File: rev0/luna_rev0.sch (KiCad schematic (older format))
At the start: 35 parts, among them J1 USB_B_Micro, J2 USB_B_Micro, J3 USB_A, J4 USB_B_Micro, J7 Conn_02x02_Counter_Clockwise, J8 Conn_Coaxial, J9 Conn_Coaxial, SW1 BTN_RECOVERY, SW2 BTN_DFU, SW3 BTN_RESET, U1 AP22814-SOT, U12 AP22814-SOT, Y1 DSC60xx

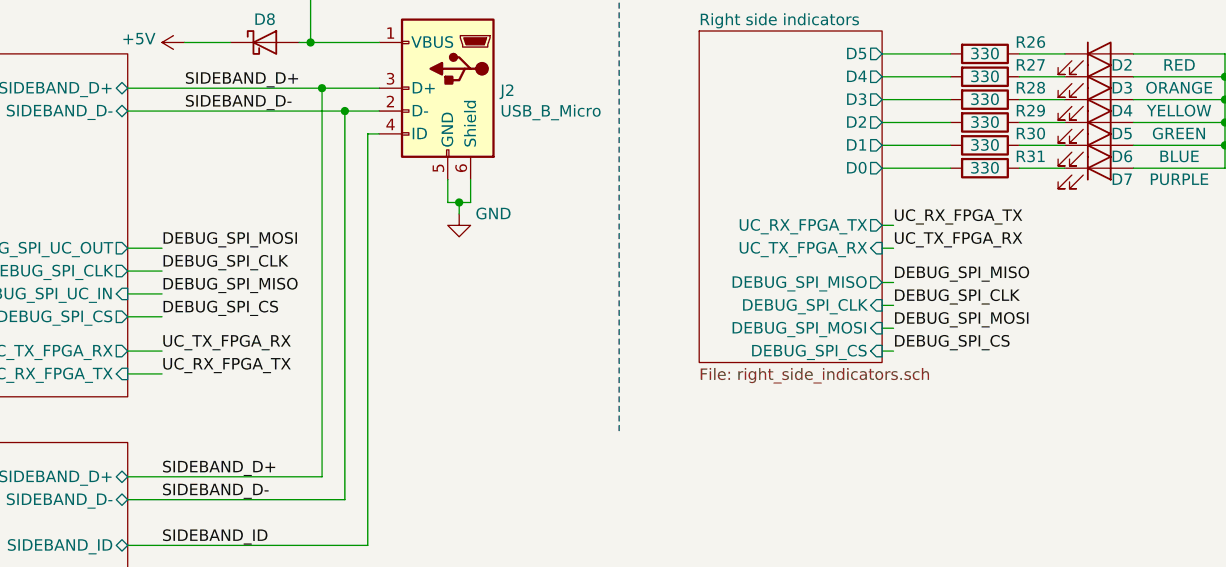
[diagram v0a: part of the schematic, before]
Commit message: hardware: adopt OSHWA convention for SPI signal names
https://www.oshwa.org/a-resolution-to-redefine-spi-signal-names
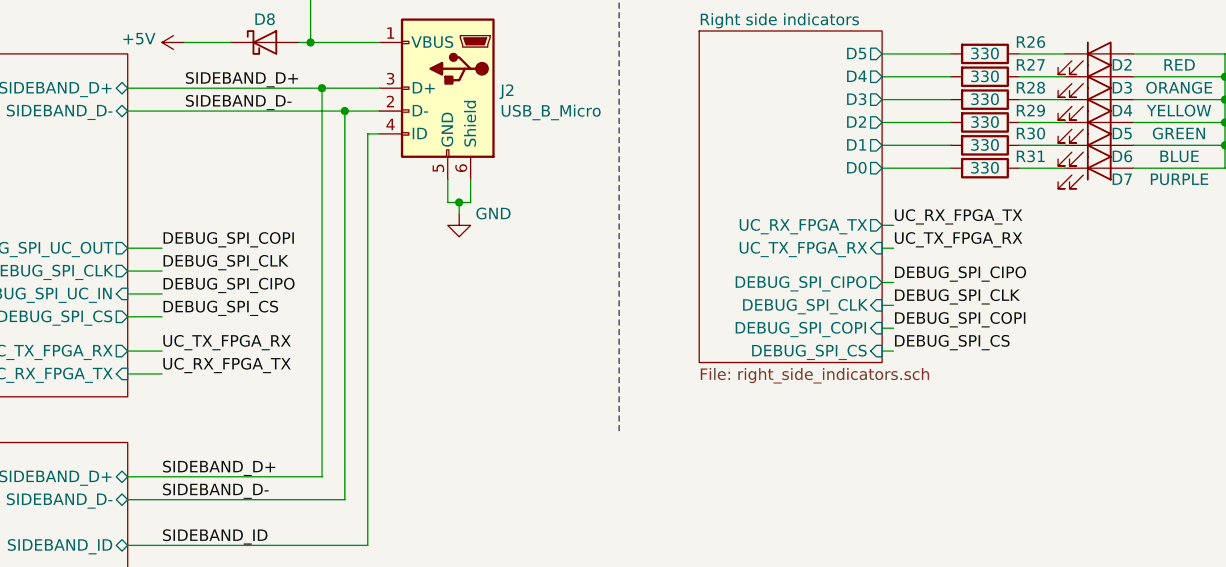
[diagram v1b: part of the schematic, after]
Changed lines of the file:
@@
 	5700 5750 5850 5750
 Text Label 5850 5750 0    50   ~ 0
-DEBUG_SPI_MOSI
+DEBUG_SPI_COPI
 Wire Wire Line
 	5700 5850 5850 5850
@@
 	5700 5950 5850 5950
 Text Label 5850 5950 0    50   ~ 0
-DEBUG_SPI_MISO
+DEBUG_SPI_CIPO
 Text Label 5850 5850 0    50   ~ 0
 DEBUG_SPI_CLK
@@
 TARGET_FAULT
 Text Label 9050 6100 0    50   ~ 0
-DEBUG_SPI_MOSI
+DEBUG_SPI_COPI
 $Comp
 L Device:R R26
@@
 F8 "UC_RX_FPGA_TX" O R 9000 5650 50
 F9 "UC_TX_FPGA_RX" I R 9000 5750 50
-F10 "DEBUG_SPI_MISO" O R 9000 5900 50
+F10 "DEBUG_SPI_CIPO" O R 9000 5900 50
 F11 "DEBUG_SPI_CLK" I R 9000 6000 50
-F12 "DEBUG_SPI_MOSI" I R 9000 6100 50
+F12 "DEBUG_SPI_COPI" I R 9000 6100 50
 F13 "DEBUG_SPI_CS" I R 9000 6200 50
 $EndSheet
@@
 DEBUG_SPI_CLK
 Text Label 9050 5900 0    50   ~ 0
-DEBUG_SPI_MISO
+DEBUG_SPI_CIPO
 Text Label 9050 6200 0    50   ~ 0
 DEBUG_SPI_CS

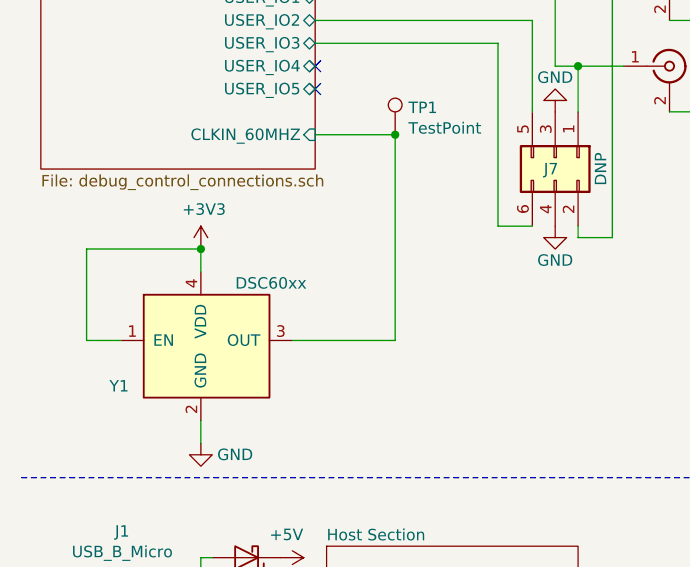
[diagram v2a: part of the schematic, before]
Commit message: hardware: replace Y1 DSC6001MI2A-060.0000 with SIT1602BC-73-33E-60.000000E
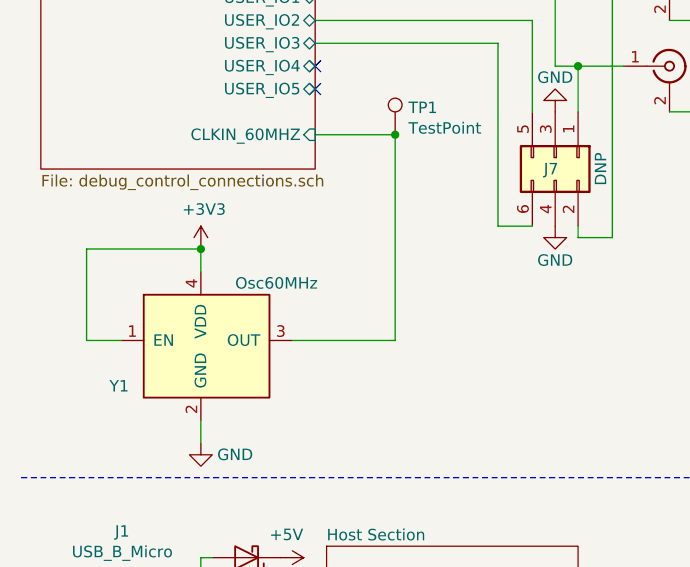
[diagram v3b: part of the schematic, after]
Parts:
- Y1: value DSC60xx -> Osc60MHz; Description MEMS OSC XO 60.0000MHZ CMOS SMD -> MEMS OSC XO 60.0000MHZ H/LV-CMOS; Manufacturer Microchip -> SiTIME; Part Number DSC6001MI2A-060.0000 -> SIT1602BC-73-33E-60.000000E
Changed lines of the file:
@@
 P 1050 2400
 F 0 "Y1" H 900 2000 50  0000 L CNN
-F 1 "DSC60xx" H 1450 2450 50  0000 L CNN
+F 1 "Osc60MHz" H 1450 2450 50  0000 L CNN
 F 2 "Crystal:Crystal_SMD_2016-4Pin_2.0x1.6mm" H 1050 2400 50  0001 C CNN
 F 3 "" H 1050 2400 50  0001 C CNN
-F 4 "MEMS OSC XO 60.0000MHZ CMOS SMD" H 1050 2400 50  0001 C CNN "Description"
-F 5 "Microchip" H 1050 2400 50  0001 C CNN "Manufacturer"
-F 6 "DSC6001MI2A-060.0000" H 1050 2400 50  0001 C CNN "Part Number"
+F 4 "MEMS OSC XO 60.0000MHZ H/LV-CMOS" H 1050 2400 50  0001 C CNN "Description"
+F 5 "SiTIME" H 1050 2400 50  0001 C CNN "Manufacturer"
+F 6 "SIT1602BC-73-33E-60.000000E" H 1050 2400 50  0001 C CNN "Part Number"
 	1    1050 2400
 	1    0    0    -1

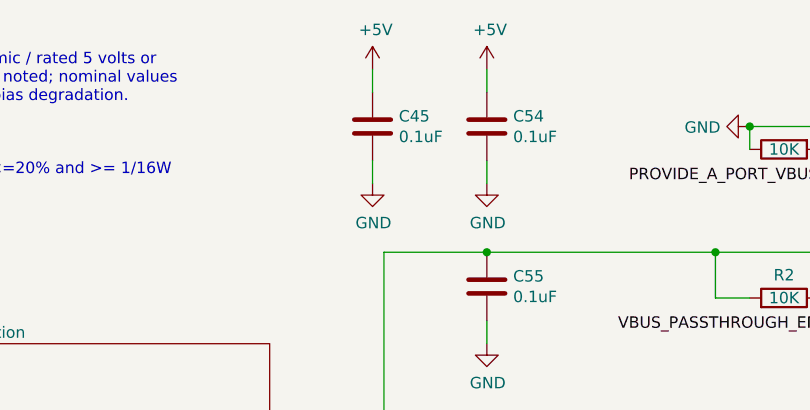
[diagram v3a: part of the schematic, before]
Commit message: hardware: remove redundant C45
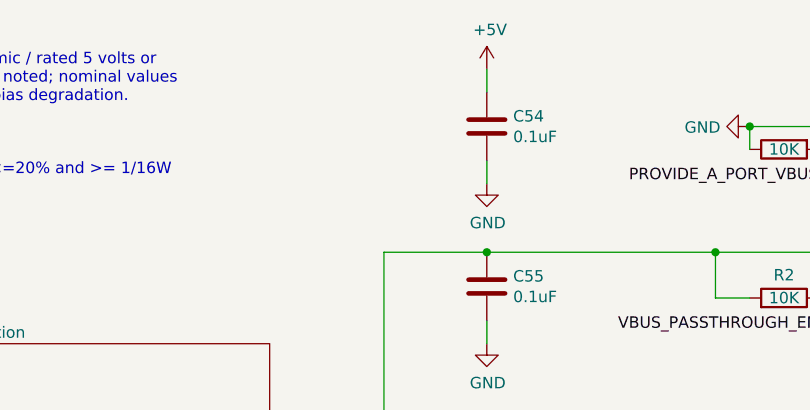
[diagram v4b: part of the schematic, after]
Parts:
- removed C45: 0.1uF, Capacitor_SMD:C_0402_1005Metric, symbol Device:C
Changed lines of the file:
@@
 Wire Wire Line
 	5850 6050 5700 6050
-$Comp
-L Device:C C45
-U 1 1 5EE7CC33
-P 6150 950
-F 0 "C45" H 6265 995 50  0000 L CNN
-F 1 "0.1uF" H 6265 905 50  0000 L CNN
-F 2 "Capacitor_SMD:C_0402_1005Metric" H 6188 800 50  0001 C CNN
-F 3 "~" H 6150 950 50  0001 C CNN
-F 4 "GENERIC-CAP-0402-0.1uF" H 6150 950 50  0001 C CNN "Part Number"
-	1    6150 950
-	1    0    0    -1
-$EndComp
-$Comp
-L power:GND #PWR0122
-U 1 1 5EE7CC3D
-P 6150 1200
-F 0 "#PWR0122" H 6150 950 50  0001 C CNN
-F 1 "GND" H 6154 1028 50  0000 C CNN
-F 2 "" H 6150 1200 50  0001 C CNN
-F 3 "" H 6150 1200 50  0001 C CNN
-	1    6150 1200
-	1    0    0    -1
-$EndComp
-Wire Wire Line
-	6150 1200 6150 1100
-$Comp
-L power:+5V #PWR0123
-U 1 1 5EE7CC48
-P 6150 700
-F 0 "#PWR0123" H 6150 550 50  0001 C CNN
-F 1 "+5V" H 6164 873 50  0000 C CNN
-F 2 "" H 6150 700 50  0001 C CNN
-F 3 "" H 6150 700 50  0001 C CNN
-	1    6150 700
-	1    0    0    -1
-$EndComp
-Wire Wire Line
-	6150 700  6150 800
 Text Notes 4050 850  0    50   ~ 0
 All caps ceramic / rated 5 volts or\nhigher unless noted; nominal values\nare post-DC-bias degradation.

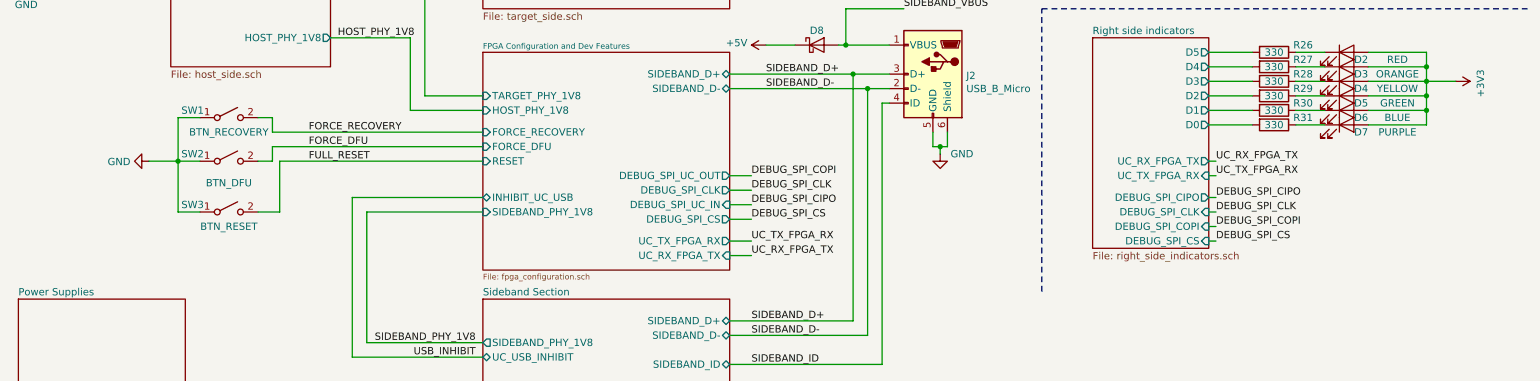
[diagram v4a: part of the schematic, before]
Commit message: hardware: replace U6 ATSAMD21 with ATSAMD11
remove FORCE_RECOVERY button
renumber button references
remove FPGA connections to U6 and replace with test points:
    CS_DI
    FPGA_CONFIG_CLK
    FPGA_DONE
    FPGA_INIT
    DEBUG_SPI_MISO
    DEBUG_SPI_MOSI
    DEBUG_SPI_CLK
    DEBUG_SPI_CS
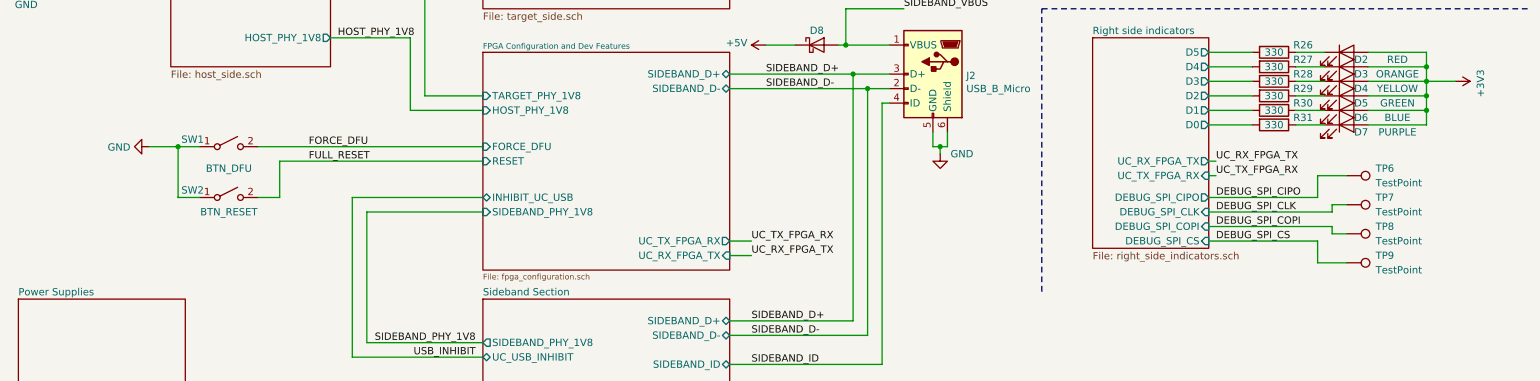
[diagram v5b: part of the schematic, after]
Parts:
- removed SW1: BTN_RECOVERY, luna:SWITCH-FSMRA, symbol Switch:SW_SPST
- added TP6, TP7, TP8, TP9: TestPoint, TestPoint:TestPoint_Pad_D1.0mm, symbol Connector:TestPoint
- renumbered SW2 to SW1, SW3 to SW2
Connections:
- net DEBUG_SPI_CIPO: now also TP6.1
- net DEBUG_SPI_CLK: now also TP7.1
- net DEBUG_SPI_COPI: now also TP8.1
- net DEBUG_SPI_CS: now also TP9.1
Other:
- moved on the sheet: SW1, SW2
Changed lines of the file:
@@
 F2 "SIDEBAND_D-" B R 5700 5150 50
 F3 "SIDEBAND_D+" B R 5700 5050 50
-F4 "DEBUG_SPI_UC_OUT" O R 5700 5750 50
-F5 "DEBUG_SPI_CLK" O R 5700 5850 50
-F6 "DEBUG_SPI_UC_IN" I R 5700 5950 50
-F7 "SIDEBAND_PHY_1V8" I L 4000 6000 50
-F8 "HOST_PHY_1V8" I L 4000 5300 50
-F9 "TARGET_PHY_1V8" I L 4000 5200 50
-F10 "FORCE_RECOVERY" I L 4000 5450 50
-F11 "FORCE_DFU" I L 4000 5550 50
-F12 "INHIBIT_UC_USB" B L 4000 5900 50
-F13 "RESET" I L 4000 5650 50
-F14 "UC_TX_FPGA_RX" O R 5700 6200 50
-F15 "UC_RX_FPGA_TX" I R 5700 6300 50
-F16 "DEBUG_SPI_CS" O R 5700 6050 50
+F4 "SIDEBAND_PHY_1V8" I L 4000 6000 50
+F5 "HOST_PHY_1V8" I L 4000 5300 50
+F6 "TARGET_PHY_1V8" I L 4000 5200 50
+F7 "FORCE_DFU" I L 4000 5550 50
+F8 "INHIBIT_UC_USB" B L 4000 5900 50
+F9 "RESET" I L 4000 5650 50
+F10 "UC_TX_FPGA_RX" O R 5700 6200 50
+F11 "UC_RX_FPGA_TX" I R 5700 6300 50
 $EndSheet
 Text Label 5950 5050 0    50   ~ 0
@@
 Text Label 5850 7050 0    50   ~ 0
 SIDEBAND_ID
-Wire Wire Line
-	5700 5750 5850 5750
-Text Label 5850 5750 0    50   ~ 0
-DEBUG_SPI_COPI
-Wire Wire Line
-	5700 5850 5850 5850
-Wire Wire Line
-	5700 5950 5850 5950
-Text Label 5850 5950 0    50   ~ 0
-DEBUG_SPI_CIPO
-Text Label 5850 5850 0    50   ~ 0
-DEBUG_SPI_CLK
 $Comp
 L support_hardware:DSC60xx Y1
@@
 $Comp
 L Switch:SW_SPST SW1
-U 1 1 5E0E58AB
-P 2250 5350
-F 0 "SW1" H 2000 5400 50  0000 C CNN
-F 1 "BTN_RECOVERY" H 2250 5250 50  0000 C CNN
-F 2 "luna:SWITCH-FSMRA" H 2250 5350 50  0001 C CNN
-F 3 "~" H 2250 5350 50  0001 C CNN
-F 4 "SWITCH TACTILE SPST-NO 0.05A 24V" H 2250 5350 50  0001 C CNN "Description"
-F 5 "TE Connectivity" H 2250 5350 50  0001 C CNN "Manufacturer"
-F 6 "1825027-5" H 2250 5350 50  0001 C CNN "Part Number"
-	1    2250 5350
-	1    0    0    -1
-$EndComp
-$Comp
-L Switch:SW_SPST SW2
 U 1 1 5E0E6B65
-P 2250 5650
-F 0 "SW2" H 2000 5700 50  0000 C CNN
-F 1 "BTN_DFU" H 2250 5500 50  0000 C CNN
-F 2 "luna:SWITCH-FSMRA" H 2250 5650 50  0001 C CNN
-F 3 "~" H 2250 5650 50  0001 C CNN
-F 4 "SWITCH TACTILE SPST-NO 0.05A 24V" H 2250 5650 50  0001 C CNN "Description"
-F 5 "TE Connectivity" H 2250 5650 50  0001 C CNN "Manufacturer"
-F 6 "1825027-5" H 2250 5650 50  0001 C CNN "Part Number"
-	1    2250 5650
-	1    0    0    -1
-$EndComp
-Wire Wire Line
-	4000 5450 2550 5450
-Wire Wire Line
-	2450 5650 2550 5650
-Wire Wire Line
-	2550 5650 2550 5550
-Wire Wire Line
-	2550 5550 4000 5550
-Wire Wire Line
-	1900 5650 2050 5650
-Wire Wire Line
-	2450 5350 2550 5350
-Wire Wire Line
-	2550 5350 2550 5450
-Wire Wire Line
-	2050 5350 1900 5350
-Text Label 2800 5450 0    50   ~ 0
-FORCE_RECOVERY
+P 2250 5550
+F 0 "SW1" H 2000 5600 50  0000 C CNN
+F 1 "BTN_DFU" H 2250 5400 50  0000 C CNN
+F 2 "luna:SWITCH-FSMRA" H 2250 5550 50  0001 C CNN
+F 3 "~" H 2250 5550 50  0001 C CNN
+F 4 "SWITCH TACTILE SPST-NO 0.05A 24V" H 2250 5550 50  0001 C CNN "Description"
+F 5 "TE Connectivity" H 2250 5550 50  0001 C CNN "Manufacturer"
+F 6 "1825027-5" H 2250 5550 50  0001 C CNN "Part Number"
+	1    2250 5550
+	1    0    0    -1
+$EndComp
+Wire Wire Line
+	2450 5550 4000 5550
+Wire Wire Line
+	1900 5550 2050 5550
 Text Label 2800 5550 0    50   ~ 0
 FORCE_DFU
@@
 TARGET_PHY_1V8
 $Comp
-L Switch:SW_SPST SW3
+L Switch:SW_SPST SW2
 U 1 1 5E2B35A7
-P 2250 6000
-F 0 "SW3" H 2000 6050 50  0000 C CNN
-F 1 "BTN_RESET" H 2250 5900 50  0000 C CNN
-F 2 "luna:SWITCH-FSMRA" H 2250 6000 50  0001 C CNN
-F 3 "~" H 2250 6000 50  0001 C CNN
-F 4 "SWITCH TACTILE SPST-NO 0.05A 24V" H 2250 6000 50  0001 C CNN "Description"
-F 5 "TE Connectivity" H 2250 6000 50  0001 C CNN "Manufacturer"
-F 6 "1825027-5" H 2250 6000 50  0001 C CNN "Part Number"
-	1    2250 6000
+P 2250 5900
+F 0 "SW2" H 2000 5950 50  0000 C CNN
+F 1 "BTN_RESET" H 2250 5800 50  0000 C CNN
+F 2 "luna:SWITCH-FSMRA" H 2250 5900 50  0001 C CNN
+F 3 "~" H 2250 5900 50  0001 C CNN
+F 4 "SWITCH TACTILE SPST-NO 0.05A 24V" H 2250 5900 50  0001 C CNN "Description"
+F 5 "TE Connectivity" H 2250 5900 50  0001 C CNN "Manufacturer"
+F 6 "1825027-5" H 2250 5900 50  0001 C CNN "Part Number"
+	1    2250 5900
 	1    0    0    -1
 $EndComp
@@
 FULL_RESET
 Wire Wire Line
-	1900 5650 1900 6000
-Wire Wire Line
-	1900 6000 2050 6000
-Connection ~ 1900 5650
-Wire Wire Line
-	2600 5650 2600 6000
+	1900 5550 1900 5900
+Wire Wire Line
+	1900 5900 2050 5900
+Connection ~ 1900 5550
 Wire Wire Line
 	2600 5650 4000 5650
 Wire Wire Line
-	2450 6000 2600 6000
-Wire Wire Line
-	1900 5350 1900 5650
+	2450 5900 2600 5900
 $Comp
 L power:GND #PWR0102
 U 1 1 5E2DCA26
-P 1700 5650
-F 0 "#PWR0102" H 1700 5400 50  0001 C CNN
-F 1 "GND" V 1704 5522 50  0000 R CNN
-F 2 "" H 1700 5650 50  0001 C CNN
-F 3 "" H 1700 5650 50  0001 C CNN
-	1    1700 5650
-	0    1    1    0
-$EndComp
-Wire Wire Line
-	1700 5650 1900 5650
+P 1700 5550
+F 0 "#PWR0102" H 1700 5300 50  0001 C CNN
+F 1 "GND" V 1704 5422 50  0000 R CNN
+F 2 "" H 1700 5550 50  0001 C CNN
+F 3 "" H 1700 5550 50  0001 C CNN
+	1    1700 5550
+	0    1    1    0
+$EndComp
+Wire Wire Line
+	1700 5550 1900 5550
 $Comp
 L power:GND #PWR0104
@@
 Wire Wire Line
 	9000 5750 9050 5750
-Wire Wire Line
-	9050 5900 9000 5900
-Wire Wire Line
-	9000 6000 9050 6000
-Wire Wire Line
-	9050 6100 9000 6100
 Wire Notes Line
 	7850 6550 7850 4600
@@
 Text Label 9050 6200 0    50   ~ 0
 DEBUG_SPI_CS
-Wire Wire Line
-	9000 6200 9050 6200
-Text Label 5850 6050 0    50   ~ 0
-DEBUG_SPI_CS
-Wire Wire Line
-	5850 6050 5700 6050
 Text Notes 4050 850  0    50   ~ 0
 All caps ceramic / rated 5 volts or\nhigher unless noted; nominal values\nare post-DC-bias degradation.
 Text Notes 4050 1250 0    50   ~ 0
 All resistors <=20% and >= 1/16W\nunless noted.
+Wire Wire Line
+	2600 5650 2600 5900
+$Comp
+L Connector:TestPoint TP6
+U 1 1 6015B9C4
+P 9950 5750
+F 0 "TP6" V 10000 5950 50  0000 L CNN
+F 1 "TestPoint" V 9900 5950 50  0000 L CNN
+F 2 "TestPoint:TestPoint_Pad_D1.0mm" H 10150 5750 50  0001 C CNN
+F 3 "~" H 10150 5750 50  0001 C CNN
+	1    9950 5750
+	0    1    -1   0
+$EndComp
+$Comp
+L Connector:TestPoint TP7
+U 1 1 6017ECBE
+P 9950 5950
+F 0 "TP7" V 10000 6150 50  0000 L CNN
+F 1 "TestPoint" V 9900 6150 50  0000 L CNN
+F 2 "TestPoint:TestPoint_Pad_D1.0mm" H 10150 5950 50  0001 C CNN
+F 3 "~" H 10150 5950 50  0001 C CNN
+	1    9950 5950
+	0    1    -1   0
+$EndComp
+$Comp
+L Connector:TestPoint TP8
+U 1 1 6018ADB4
+P 9950 6150
+F 0 "TP8" V 10000 6350 50  0000 L CNN
+F 1 "TestPoint" V 9900 6350 50  0000 L CNN
+F 2 "TestPoint:TestPoint_Pad_D1.0mm" H 10150 6150 50  0001 C CNN
+F 3 "~" H 10150 6150 50  0001 C CNN
+	1    9950 6150
+	0    1    -1   0
+$EndComp
+$Comp
+L Connector:TestPoint TP9
+U 1 1 6018ADBE
+P 9950 6350
+F 0 "TP9" V 10000 6550 50  0000 L CNN
+F 1 "TestPoint" V 9900 6550 50  0000 L CNN
+F 2 "TestPoint:TestPoint_Pad_D1.0mm" H 10150 6350 50  0001 C CNN
+F 3 "~" H 10150 6350 50  0001 C CNN
+	1    9950 6350
+	0    1    -1   0
+$EndComp
+Wire Wire Line
+	9000 6000 9850 6000
+Wire Wire Line
+	9850 6000 9850 5950
+Wire Wire Line
+	9850 5950 9950 5950
+Wire Wire Line
+	9000 6100 9850 6100
+Wire Wire Line
+	9850 6100 9850 6150
+Wire Wire Line
+	9850 6150 9950 6150
+Wire Wire Line
+	9000 6200 9750 6200
+Wire Wire Line
+	9750 6200 9750 6350
+Wire Wire Line
+	9750 6350 9950 6350
+Wire Wire Line
+	9000 5900 9750 5900
+Wire Wire Line
+	9750 5900 9750 5750
+Wire Wire Line
+	9750 5750 9950 5750
 $EndSCHEMATC
